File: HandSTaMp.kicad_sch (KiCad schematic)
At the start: 24 parts, among them J1 USB_C_Receptacle_USB2.0_16P, J2 Pins, J3 SWD, SW0 BOOT, SW1 Row 0, Col 0, SW2 Row 0, Col 1, U1 STM32C071GBUx, U2 PRTR5V0U2X, U3 XC6206P332MR-G

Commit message: Tweak routing, especially R1 and C0
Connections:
- net C0: now also U1.16 (PA8); no longer U1.17 (PC6)
- net R0: now also U1.17 (PC6); no longer U1.16 (PA8)
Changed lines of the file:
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@@
 		)
 	)
-	(global_label "C0"
+	(global_label "R0"
 		(shape input)
 		(at 179.07 40.64 180)
@@
 		)
 		(property "Intersheetrefs" "${INTERSHEET_REFS}"
-			(at 174.3146 40.64 0)
+			(at 174.2029 40.64 0)
 			(hide yes)
 			(show_name no)
@@
 		)
 	)
-	(global_label "R0"
+	(global_label "C0"
 		(shape input)
 		(at 199.39 55.88 0)
@@
 		)
 		(property "Intersheetrefs" "${INTERSHEET_REFS}"
-			(at 204.2571 55.88 0)
-			(hide yes)
-			(show_name no)
+			(at 204.1454 55.88 0)
+			(hide yes)
+			(show_name no)

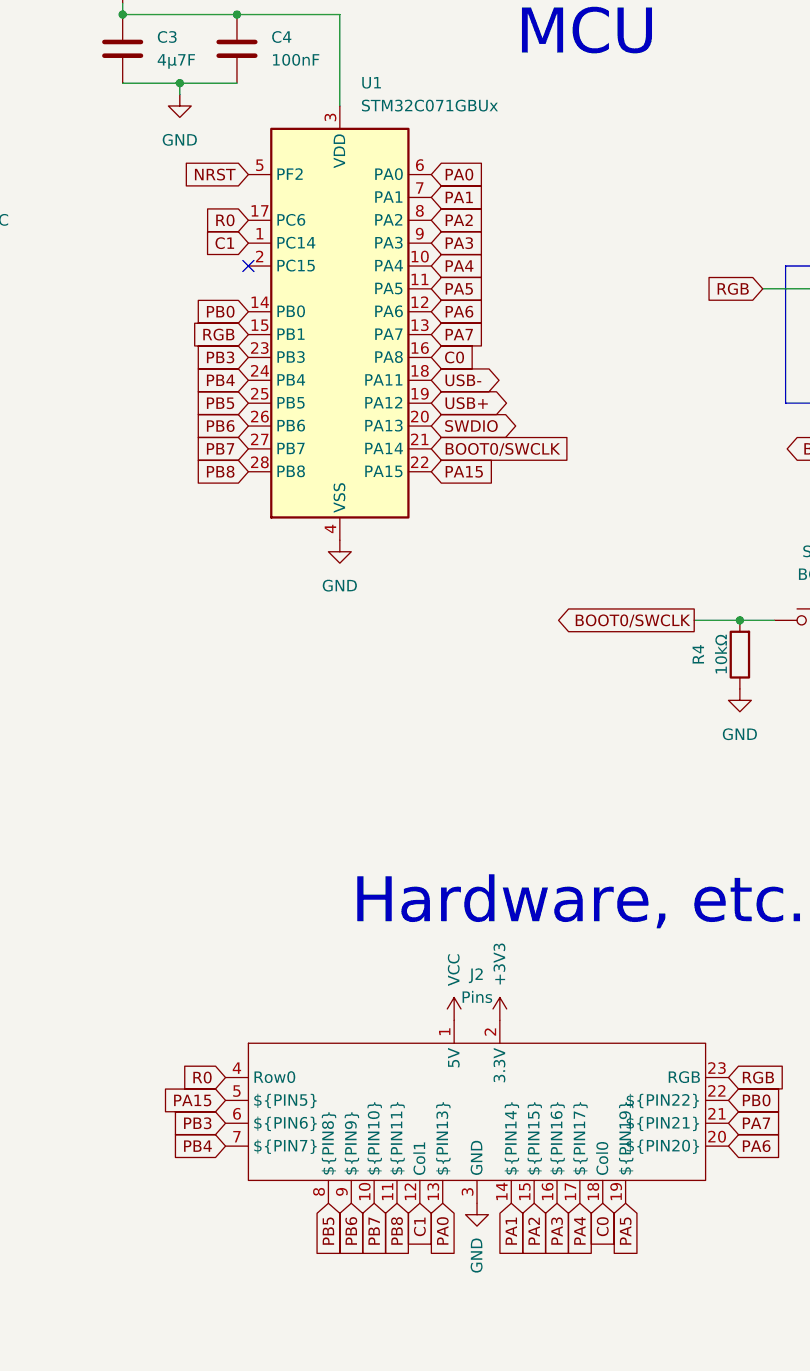
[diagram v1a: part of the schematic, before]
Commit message: Swap column pins to edge of group
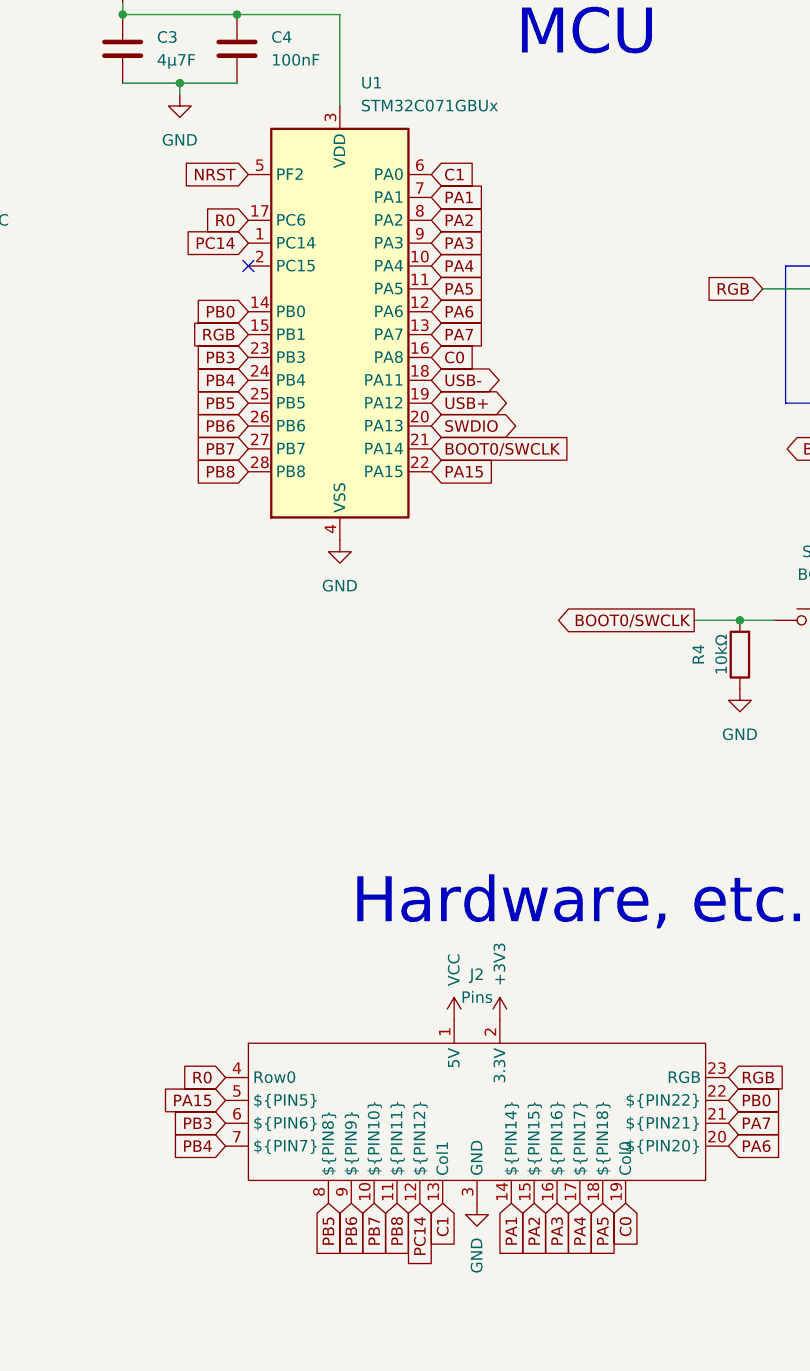
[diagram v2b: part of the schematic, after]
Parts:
- J2: PIN12 (none) -> C14; PIN13 A0 -> (none); PIN18 (none) -> A5; PIN19 A5 -> (none)
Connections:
- net PA0 is gone; now on net C1: J2.13 (Col1), U1.6 (PA0)
- net C0: now also J2.19 (Col0); no longer J2.18 (Col0)
- net C1: no longer J2.12 (Col1), U1.1 (PC14)
- net PA5: now also J2.18 (${PIN18}); no longer J2.19 (${PIN19})
- new net PC14: J2.12 (${PIN12}), U1.1 (PC14)
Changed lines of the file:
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@@
 		)
 	)
-	(global_label "PA0"
+	(global_label "PB0"
 		(shape input)
-		(at 200.66 149.86 270)
+		(at 232.41 138.43 0)
 		(fields_autoplaced yes)
 		(effects
@@
 				(size 1.27 1.27)
 			)
-			(justify right)
+			(justify left)
 		)
 		(property "Intersheetrefs" "${INTERSHEET_REFS}"
-			(at 200.66 155.603 90)
+			(at 238.3305 138.43 0)
 			(hide yes)
 			(show_name no)
@@
 					(size 1.27 1.27)
 				)
-				(justify right)
+				(justify left)
 			)
 		)
 	)
-	(global_label "PB0"
+	(global_label "R0"
 		(shape input)
-		(at 232.41 138.43 0)
+		(at 179.07 40.64 180)
 		(fields_autoplaced yes)
 		(effects
@@
 				(size 1.27 1.27)
 			)
-			(justify left)
+			(justify right)
 		)
 		(property "Intersheetrefs" "${INTERSHEET_REFS}"
-			(at 238.3305 138.43 0)
+			(at 174.2029 40.64 0)
 			(hide yes)
 			(show_name no)
@@
 					(size 1.27 1.27)
 				)
-				(justify left)
+				(justify right)
 			)
 		)
 	)
-	(global_label "R0"
+	(global_label "PC14"
 		(shape input)
-		(at 179.07 40.64 180)
+		(at 179.07 43.18 180)
 		(fields_autoplaced yes)
 		(effects
@@
 		)
 		(property "Intersheetrefs" "${INTERSHEET_REFS}"
-			(at 174.2029 40.64 0)
+			(at 172.5068 43.18 0)
 			(hide yes)
 			(show_name no)
@@
 	(global_label "C0"
 		(shape input)
-		(at 218.44 149.86 270)
+		(at 220.98 149.86 270)
 		(fields_autoplaced yes)
 		(effects
@@
 		)
 		(property "Intersheetrefs" "${INTERSHEET_REFS}"
-			(at 218.44 155.3247 90)
+			(at 220.98 155.3247 90)
 			(hide yes)
 			(show_name no)
@@
 	(global_label "PA5"
 		(shape input)
-		(at 220.98 149.86 270)
+		(at 218.44 149.86 270)
 		(fields_autoplaced yes)
 		(effects
@@
 		)
 		(property "Intersheetrefs" "${INTERSHEET_REFS}"
-			(at 220.98 155.5087 90)
+			(at 218.44 155.5087 90)
 			(hide yes)
 			(show_name no)
@@
 		)
 	)
-	(global_label "PA0"
-		(shape input)
-		(at 199.39 35.56 0)
-		(fields_autoplaced yes)
-		(effects
-			(font
-				(size 1.27 1.27)
-			)
-			(justify left)
-		)
-		(property "Intersheetrefs" "${INTERSHEET_REFS}"
-			(at 205.133 35.56 0)
-			(hide yes)
-			(show_name no)
-			(do_not_autoplace no)
-			(effects
-				(font
-					(size 1.27 1.27)
-				)
-				(justify left)
-			)
-		)
-	)
 	(global_label "USB-"
 		(shape bidirectional)
@@
 	(global_label "C1"
 		(shape input)
-		(at 198.12 149.86 270)
+		(at 200.66 149.86 270)
 		(fields_autoplaced yes)
 		(effects
@@
 		)
 		(property "Intersheetrefs" "${INTERSHEET_REFS}"
-			(at 198.12 155.3247 90)
+			(at 200.66 155.3247 90)
 			(hide yes)
 			(show_name no)
@@
 		)
 	)
-	(global_label "PB7"
+	(global_label "PC14"
 		(shape input)
-		(at 193.04 149.86 270)
+		(at 198.12 149.86 270)
 		(fields_autoplaced yes)
 		(effects
@@
 		)
 		(property "Intersheetrefs" "${INTERSHEET_REFS}"
-			(at 193.04 155.5733 90)
+			(at 198.12 156.4232 90)
 			(hide yes)
 			(show_name no)
@@
 		)
 	)
-	(global_label "C1"
+	(global_label "PB7"
 		(shape input)
-		(at 179.07 43.18 180)
+		(at 193.04 149.86 270)
 		(fields_autoplaced yes)
 		(effects
@@
 		)
 		(property "Intersheetrefs" "${INTERSHEET_REFS}"
-			(at 174.5342 43.18 0)
+			(at 193.04 155.5733 90)
 			(hide yes)
 			(show_name no)
@@
 		)
 	)
+	(global_label "C1"
+		(shape input)
+		(at 199.39 35.56 0)
+		(fields_autoplaced yes)
+		(effects
+			(font
+				(size 1.27 1.27)
+			)
+			(justify left)
+		)
+		(property "Intersheetrefs" "${INTERSHEET_REFS}"
+			(at 203.9258 35.56 0)
+			(hide yes)
+			(show_name no)
+			(do_not_autoplace no)
+			(effects
+				(font
+					(size 1.27 1.27)
+				)
+				(justify left)
+			)
+		)
+	)
 	(netclass_flag ""
 		(length 2.54)
@@
 			)
 		)
-		(property "PIN13" "A0"
+		(property "PIN12" "C14"
 			(at 204.47 139.7 0)
 			(hide yes)
@@
 			)
 		)
-		(property "PIN19" "A5"
+		(property "PIN18" "A5"
 			(at 204.47 139.7 0)
 			(hide yes)

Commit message: Add LSCC, DigiKey and manufacturer’s part numbers
BOM could be optimised to substitute some passive components with equivalent “Basic” parts if using JLC assembly.
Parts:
- C1, C2: DigiKey (none) -> 1276-1034-1; LCSC C52923 -> C1592; MPN (none) -> CL10A105KO8NNNC
- C3: DigiKey (none) -> 1276-1784-1; LCSC (none) -> C19666; MPN (none) -> CL10A475KO8NNNC
- C4, C5: DigiKey (none) -> 1276-1005-1; LCSC (none) -> C66501; MPN (none) -> CL10B104KO8NNNC
- D1: DigiKey 1727-4326 -> 1727-4326-1; LCSC C2837790 -> C193668; MPN (none) -> PMEG2010EA,115
- D2, D3: DigiKey (none) -> 1N4148WQ-7-FDI; LCSC (none) -> C7603179; MPN (none) -> 1N4148W
- F1: DigiKey MF-FSMF050X -> MF-FSMF050X-2; MPN (none) -> MF-FSMF050X-2
- J1: DigiKey (none) -> 2223-UJ20-C-H-G-SMT-1A-P16 (untested; may be compatible); LCSC (none) -> C165948; MPN (none) -> TYPE-C-31-M-12
- J3, NT1, SW1, SW2: MPN (none) -> -
- R1, R2, R3: MPN (none) -> 0603WAF5101T5E/RC0603FR-075K1L
- R4: DigiKey 311-5.10KHR -> 311-10.0KHR; LCSC C23186 -> C25804; MPN (none) -> 0603WAF1002T5E/RC0603FR-0710KL
- R5: DigiKey 311-5.10KHR -> 311-330HR; LCSC C23186 -> C23138; MPN (none) -> 0603WAF3300T5E/RC0603FR-07330RL
- SW0: DigiKey SW1020CT-ND -> SW1020CT; MPN (none) -> B3U-1000P
- U1: DigiKey (none) -> 497-STM32C071GBU6-ND; LCSC (none) -> C42113261; MPN (none) -> STM32C071GBU6
- U2: DigiKey 1727-3884-1-ND -> 1727-3884-1; MPN (none) -> PRTR5V0U2X,215
- U3: DigiKey (none) -> 893-XC6206P332MR-G; LCSC (none) -> C5446; MPN (none) -> XC6206P332MR-G

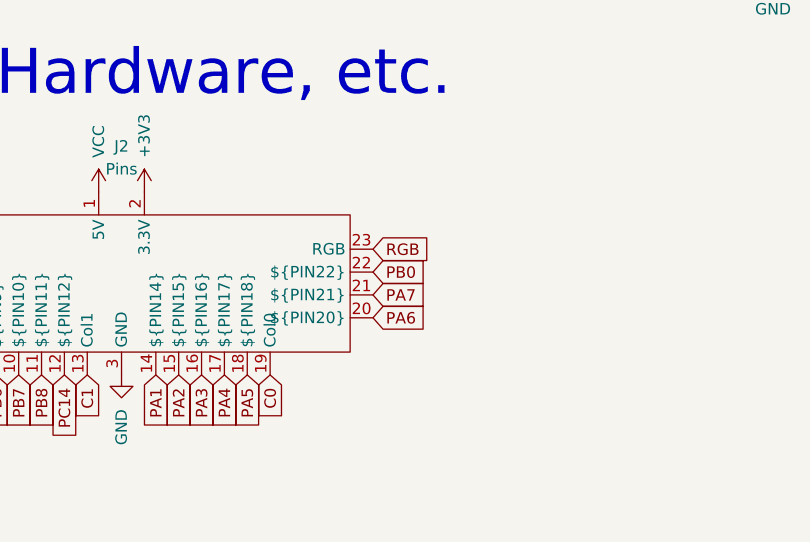
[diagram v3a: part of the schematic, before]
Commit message: Move extra pin to short side
This better avoids the switch as the left and right sides taper in a bit compared to the top and bottom sides, which are more straight.
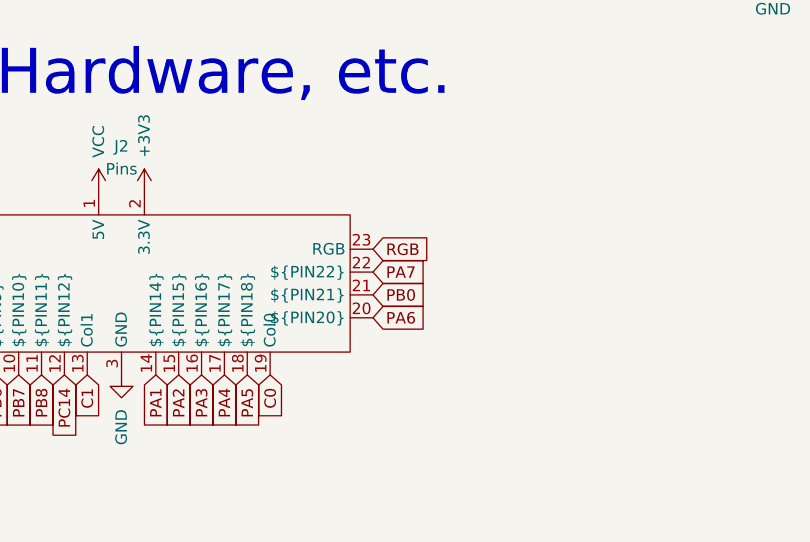
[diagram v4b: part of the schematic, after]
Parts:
- J2: PIN21 A7 -> B0; PIN22 B0 -> A7
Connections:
- net PA7: now also J2.22 (${PIN22}); no longer J2.21 (${PIN21})
- net PB0: now also J2.21 (${PIN21}); no longer J2.22 (${PIN22})
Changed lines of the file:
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@@
 	(global_label "PB0"
 		(shape input)
-		(at 232.41 138.43 0)
+		(at 232.41 140.97 0)
 		(fields_autoplaced yes)
 		(effects
@@
 		)
 		(property "Intersheetrefs" "${INTERSHEET_REFS}"
-			(at 238.3305 138.43 0)
+			(at 238.3305 140.97 0)
 			(hide yes)
 			(show_name no)
@@
 	(global_label "PA7"
 		(shape input)
-		(at 232.41 140.97 0)
+		(at 232.41 138.43 0)
 		(fields_autoplaced yes)
 		(effects
@@
 		)
 		(property "Intersheetrefs" "${INTERSHEET_REFS}"
-			(at 237.9099 140.97 0)
+			(at 237.9099 138.43 0)
 			(hide yes)
 			(show_name no)
@@
 			)
 		)
-		(property "PIN21" "A7"
+		(property "PIN21" "B0"
 			(at 204.47 139.7 0)
 			(hide yes)
@@
 			)
 		)
-		(property "PIN22" "B0"
+		(property "PIN22" "A7"
 			(at 204.47 139.7 0)
 			(hide yes)

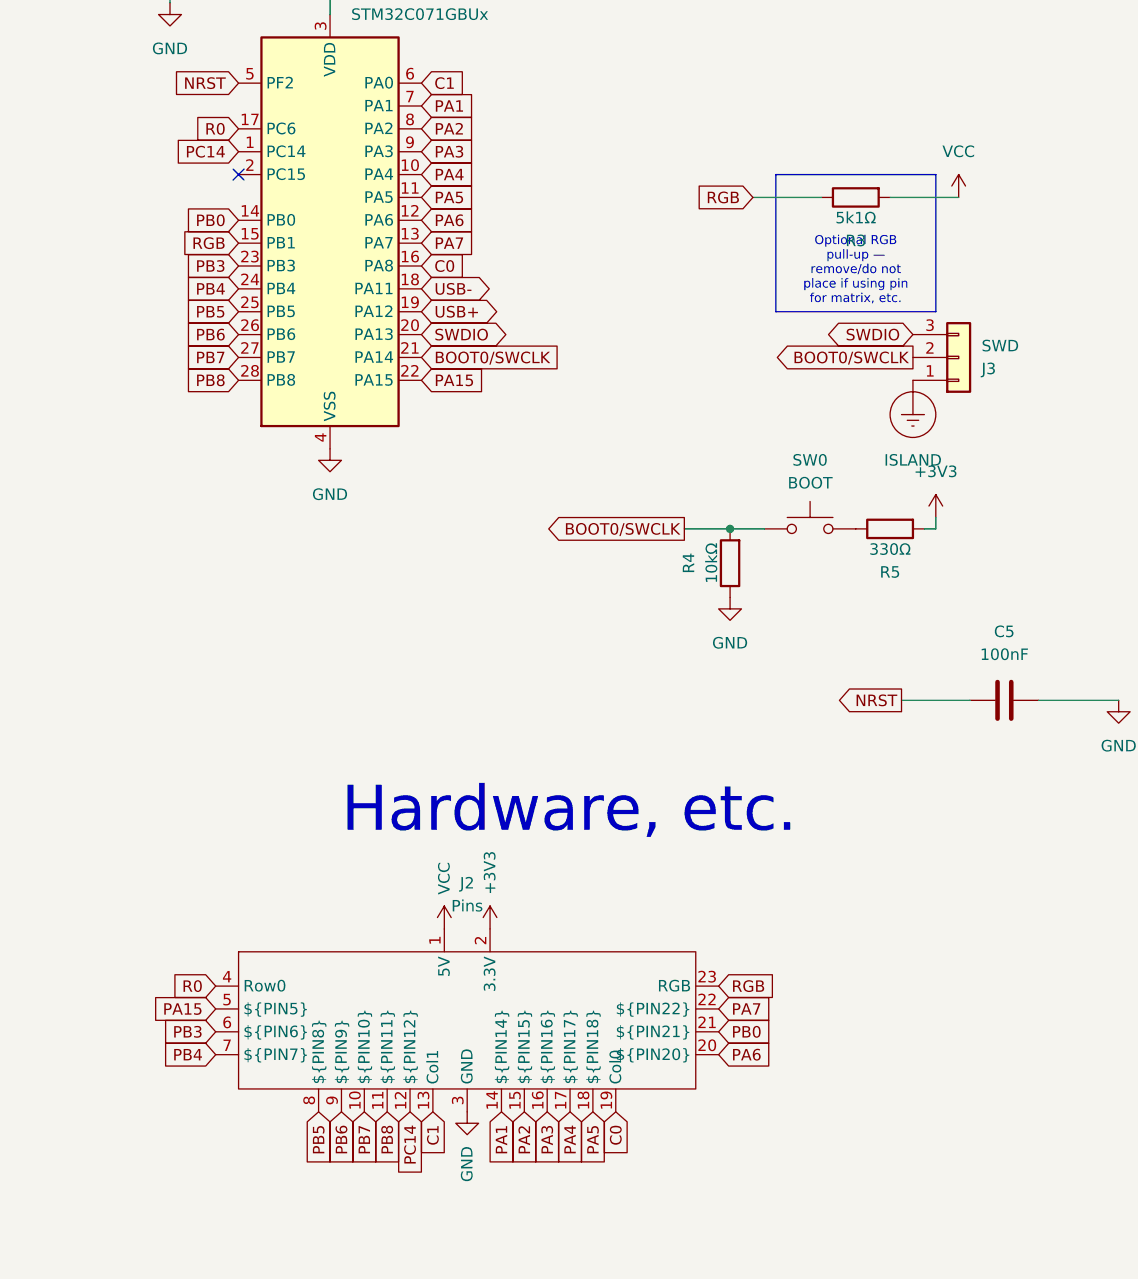
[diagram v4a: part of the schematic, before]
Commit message: Add pad for PC15 access
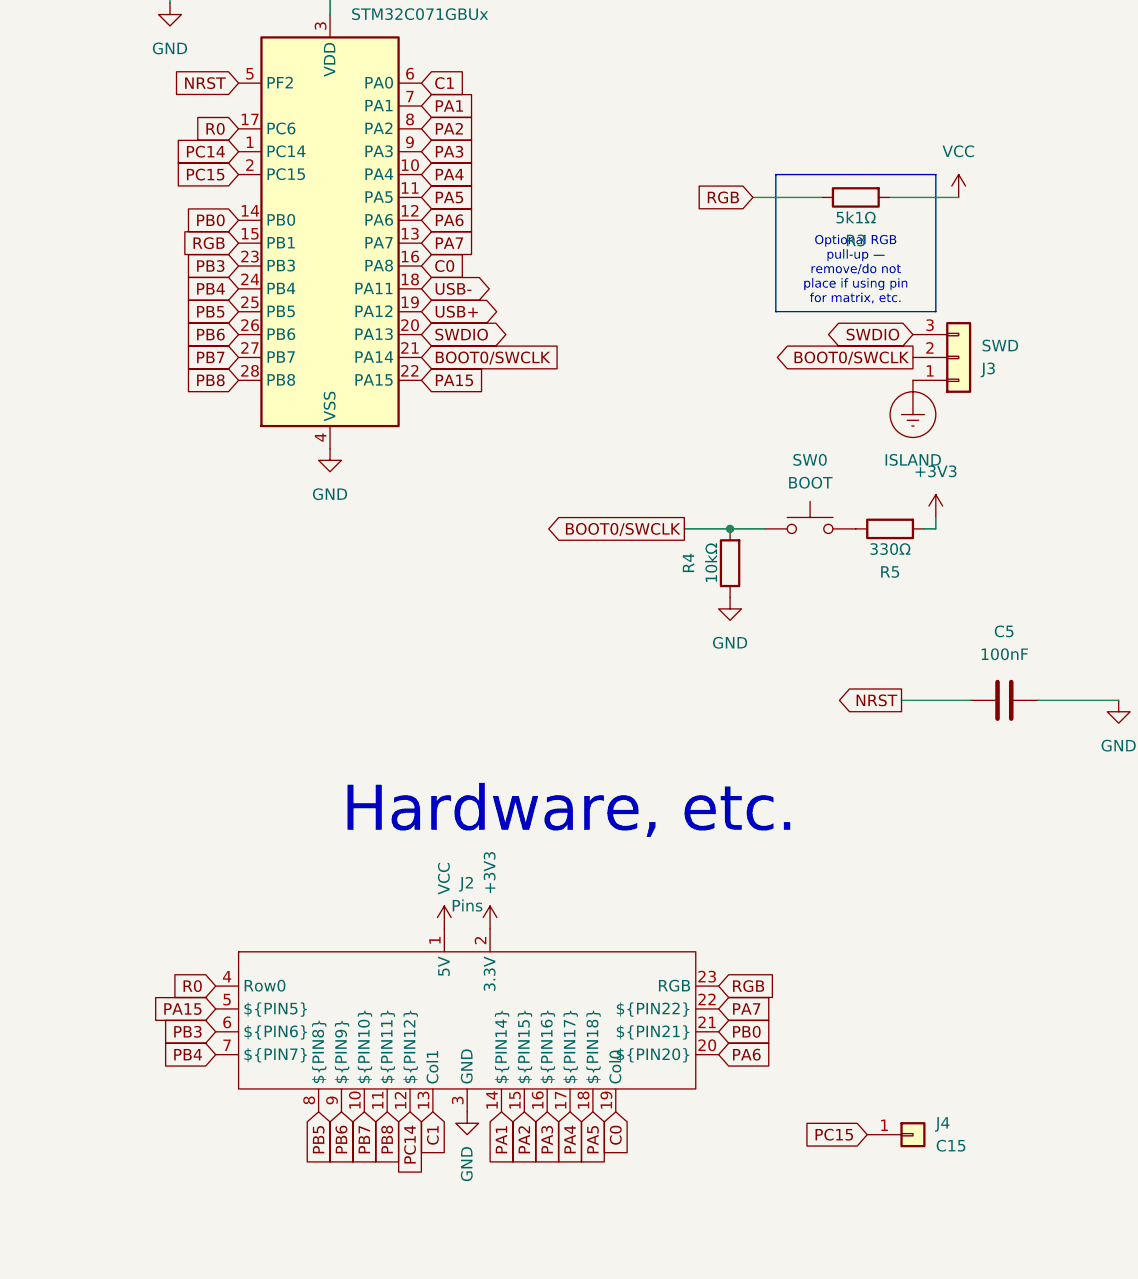
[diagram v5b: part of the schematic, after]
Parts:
- added J4: C15, Project Library:TestPoint_Pad_1.5x1.5mm, symbol Connector_Generic:Conn_01x01
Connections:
- net PC15: now reaches U1.2 (PC15)
- net PC15: now also J4.1 (Pin_1)
- no-connect marks 3 -> 2
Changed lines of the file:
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@@
 	)
 	(no_connect
-		(at 179.07 45.72)
-	)
-	(no_connect
 		(at 45.72 69.85)
 	)
@@
 		)
 	)
+	(global_label "PC15"
+		(shape input)
+		(at 248.92 152.4 180)
+		(fields_autoplaced yes)
+		(effects
+			(font
+				(size 1.27 1.27)
+			)
+			(justify right)
+		)
+		(property "Intersheetrefs" "${INTERSHEET_REFS}"
+			(at 242.4102 152.4 0)
+			(hide yes)
+			(show_name no)
+			(do_not_autoplace no)
+			(effects
+				(font
+					(size 1.27 1.27)
+				)
+				(justify right)
+			)
+		)
+	)
 	(global_label "PA4"
 		(shape input)
@@
 		)
 	)
+	(global_label "PC15"
+		(shape input)
+		(at 179.07 45.72 180)
+		(fields_autoplaced yes)
+		(effects
+			(font
+				(size 1.27 1.27)
+			)
+			(justify right)
+		)
+		(property "Intersheetrefs" "${INTERSHEET_REFS}"
+			(at 172.5602 45.72 0)
+			(hide yes)
+			(show_name no)
+			(do_not_autoplace no)
+			(effects
+				(font
+					(size 1.27 1.27)
+				)
+				(justify right)
+			)
+		)
+	)
 	(global_label "PA5"
 		(shape input)
@@
 					(unit 1)
 				)
+			)
+		)
+	)
+	(symbol
+		(lib_id "Connector_Generic:Conn_01x01")
+		(at 254 152.4 0)
+		(unit 1)
+		(body_style 1)
+		(exclude_from_sim no)
+		(in_bom yes)
+		(on_board yes)
+		(in_pos_files yes)
+		(dnp no)
+		(fields_autoplaced yes)
+		(property "Reference" "J4"
+			(at 256.54 151.13 0)
+			(show_name no)
+			(do_not_autoplace no)
+			(effects
+				(font
+					(size 1.27 1.27)
+				)
+				(justify left)
+			)
+		)
+		(property "Value" "C15"
+			(at 256.54 153.67 0)
+			(show_name no)
+			(do_not_autoplace no)
+			(effects
+				(font
+					(size 1.27 1.27)
+				)
+				(justify left)
+			)
+		)
+		(property "Footprint" "Project Library:TestPoint_Pad_1.5x1.5mm"
+			(at 254 152.4 0)
+			(hide yes)
+			(show_name no)
+			(do_not_autoplace no)
+			(effects
+				(font
+					(size 1.27 1.27)
+				)
+			)
+		)
+		(property "Datasheet" ""
+			(at 254 152.4 0)
+			(hide yes)
+			(show_name no)
+			(do_not_autoplace no)
+			(effects
+				(font
+					(size 1.27 1.27)
+				)
+			)
+		)
+		(property "Description" "Generic connector, single row, 01x01, script generated (kicad-library-utils/schlib/autogen/connector/)"
+			(at 254 152.4 0)
+			(hide yes)
+			(show_name no)
+			(do_not_autoplace no)
+			(effects
+				(font
+					(size 1.27 1.27)
+				)
+			)
+		)
+		(pin "1"
+		)
+		(instances
+			(project "HandSTaMp"
+				(path "/34400e51-cf83-464a-b3ec-e9a28a972a27"
+					(reference "J4")
+					(unit 1)
+				)
